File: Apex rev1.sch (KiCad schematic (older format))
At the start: 23 parts, among them J1 OLED, SW1 SW_PUSH, SW2 Rotary_Encoder_Switch, U1 AT90USB1286-MU, Y1 8MHz

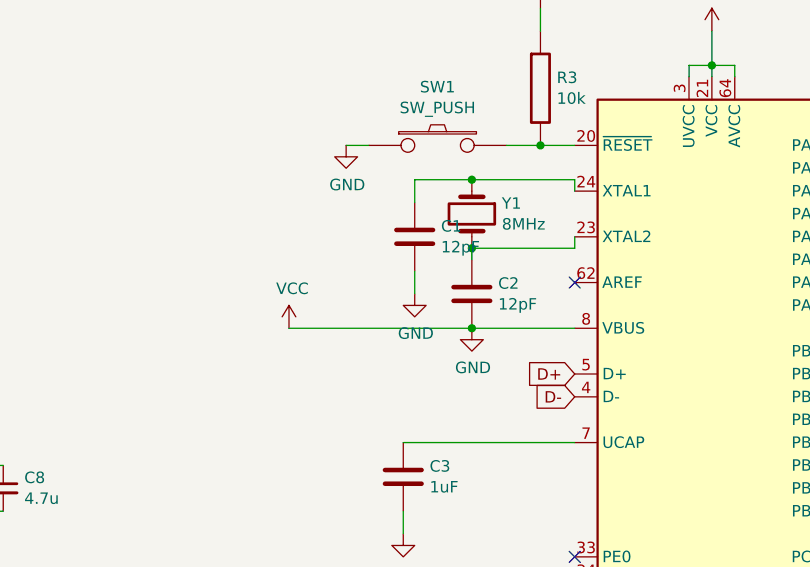
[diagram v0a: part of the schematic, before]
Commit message: Fixed symbols
Re-wired MCU XTAL and corrected footprints
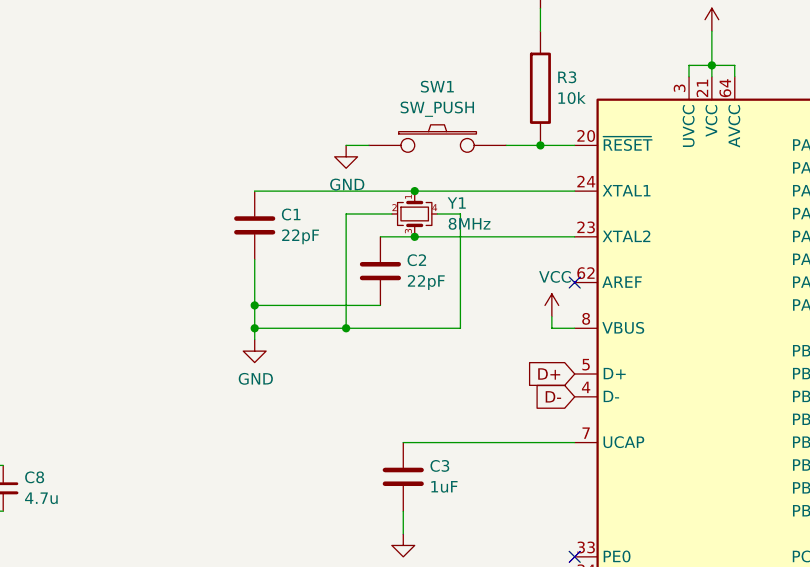
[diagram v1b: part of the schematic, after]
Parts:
- removed Y1: 8MHz, Crystal:Crystal_SMD_0603-2Pin_6.0x3.5mm, symbol Device:Crystal
- added Y1: 8MHz, Crystal:Crystal_SMD_3225-4Pin_3.2x2.5mm, symbol Device:Crystal_GND24_Small
- C1, C2: value 12pF -> 22pF
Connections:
- net GND: now also Y1.2, Y1.4; no longer C4.1, C5.1, C6.1, C7.1, C8.1, R1.1, R2.1, R26.1, R27.1, R3.1, U1.21 (VCC), U1.3 (UVCC), U1.52 (VCC), U1.64 (AVCC), U1.8 (VBUS)
- net at C2.1, U1.23 (XTAL2): now also Y1.3
- net at C1.1, U1.24 (XTAL1): now also Y1.1
- new net VCC: C4.1, C5.1, C6.1, C7.1, C8.1, R1.1, R2.1, R26.1, R27.1, R3.1, U1.21 (VCC), U1.3 (UVCC), U1.52 (VCC), U1.64 (AVCC), U1.8 (VBUS)
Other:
- moved on the sheet: C1, C2
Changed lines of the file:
@@
 	7400 1750 7500 1750
-$Comp
-L Device:Crystal Y1
-U 1 1 5F03BFD9
-P 7950 2050
-F 0 "Y1" V 7904 2181 50  0000 L CNN
-F 1 "8MHz" V 7995 2181 50  0000 L CNN
-F 2 "Crystal:Crystal_SMD_0603-2Pin_6.0x3.5mm" H 7950 2050 50  0001 C CNN
-F 3 "~" H 7950 2050 50  0001 C CNN
-	1    7950 2050
-	0    1    1    0
-$EndComp
-Wire Wire Line
-	8400 1950 8400 1900
-Wire Wire Line
-	8400 1900 7950 1900
-Wire Wire Line
-	7700 1900 7700 2000
-Connection ~ 7950 1900
-Wire Wire Line
-	7950 1900 7700 1900
-Wire Wire Line
-	8400 2150 8400 2200
-Wire Wire Line
-	8400 2200 7950 2200
-Wire Wire Line
-	7950 2200 7950 2250
-Connection ~ 7950 2200
 $Comp
 L Device:C C1
 U 1 1 5F03FC8D
-P 7700 2150
-F 0 "C1" H 7815 2196 50  0000 L CNN
-F 1 "12pF" H 7815 2105 50  0000 L CNN
-F 2 "Capacitor_SMD:C_0805_2012Metric" H 7738 2000 50  0001 C CNN
-F 3 "~" H 7700 2150 50  0001 C CNN
-	1    7700 2150
-	1    0    0    -1
-$EndComp
-Wire Wire Line
-	7700 2300 7700 2400
+P 7000 2100
+F 0 "C1" H 7115 2146 50  0000 L CNN
+F 1 "22pF" H 7115 2055 50  0000 L CNN
+F 2 "Capacitor_SMD:C_0805_2012Metric" H 7038 1950 50  0001 C CNN
+F 3 "~" H 7000 2100 50  0001 C CNN
+	1    7000 2100
+	1    0    0    -1
+$EndComp
 $Comp
 L Device:C C2
 U 1 1 5F0408BF
-P 7950 2400
-F 0 "C2" H 8065 2446 50  0000 L CNN
-F 1 "12pF" H 8065 2355 50  0000 L CNN
-F 2 "Capacitor_SMD:C_0805_2012Metric" H 7988 2250 50  0001 C CNN
-F 3 "~" H 7950 2400 50  0001 C CNN
-	1    7950 2400
-	1    0    0    -1
-$EndComp
-$Comp
-L power:GND #PWR0104
-U 1 1 5F0414EA
-P 7700 2400
-F 0 "#PWR0104" H 7700 2150 50  0001 C CNN
-F 1 "GND" H 7705 2227 50  0000 C CNN
-F 2 "" H 7700 2400 50  0001 C CNN
-F 3 "" H 7700 2400 50  0001 C CNN
-	1    7700 2400
+P 7550 2300
+F 0 "C2" H 7665 2346 50  0000 L CNN
+F 1 "22pF" H 7665 2255 50  0000 L CNN
+F 2 "Capacitor_SMD:C_0805_2012Metric" H 7588 2150 50  0001 C CNN
+F 3 "~" H 7550 2300 50  0001 C CNN
+	1    7550 2300
 	1    0    0    -1
 $EndComp
@@
 L power:GND #PWR0105
 U 1 1 5F041BDD
-P 7950 2550
-F 0 "#PWR0105" H 7950 2300 50  0001 C CNN
-F 1 "GND" H 7955 2377 50  0000 C CNN
-F 2 "" H 7950 2550 50  0001 C CNN
-F 3 "" H 7950 2550 50  0001 C CNN
-	1    7950 2550
+P 7000 2600
+F 0 "#PWR0105" H 7000 2350 50  0001 C CNN
+F 1 "GND" H 7005 2427 50  0000 C CNN
+F 2 "" H 7000 2600 50  0001 C CNN
+F 3 "" H 7000 2600 50  0001 C CNN
+	1    7000 2600
 	1    0    0    -1
 $EndComp
@@
 	1    0    0    -1
 $EndComp
-Wire Wire Line
-	8400 2550 7950 2550
-Connection ~ 7950 2550
-Wire Wire Line
-	7950 2550 7150 2550
 $Comp
 L power:VCC #PWR0112
 U 1 1 5F073B72
-P 7150 2550
-F 0 "#PWR0112" H 7150 2400 50  0001 C CNN
-F 1 "VCC" H 7165 2723 50  0000 C CNN
-F 2 "" H 7150 2550 50  0001 C CNN
-F 3 "" H 7150 2550 50  0001 C CNN
-	1    7150 2550
+P 8300 2500
+F 0 "#PWR0112" H 8300 2350 50  0001 C CNN
+F 1 "VCC" H 8315 2673 50  0000 C CNN
+F 2 "" H 8300 2500 50  0001 C CNN
+F 3 "" H 8300 2500 50  0001 C CNN
+	1    8300 2500
 	1    0    0    -1
 $EndComp
@@
 NoConn ~ 9600 2250
 NoConn ~ 9600 2350
+Wire Wire Line
+	8400 2550 8300 2550
+Wire Wire Line
+	8300 2550 8300 2500
+Wire Wire Line
+	8400 1950 7700 1950
+Wire Wire Line
+	8400 2150 7700 2150
+$Comp
+L Device:Crystal_GND24_Small Y1
+U 1 1 5F0E2CAB
+P 7700 2050
+F 0 "Y1" V 7654 2194 50  0000 L CNN
+F 1 "8MHz" V 7745 2194 50  0000 L CNN
+F 2 "Crystal:Crystal_SMD_3225-4Pin_3.2x2.5mm" H 7700 2050 50  0001 C CNN
+F 3 "~" H 7700 2050 50  0001 C CNN
+	1    7700 2050
+	0    1    1    0
+$EndComp
+Connection ~ 7700 1950
+Wire Wire Line
+	7700 1950 7000 1950
+Wire Wire Line
+	7700 2150 7550 2150
+Connection ~ 7700 2150
+Wire Wire Line
+	7000 2250 7000 2450
+Wire Wire Line
+	7550 2450 7000 2450
+Wire Wire Line
+	7000 2450 7000 2550
+Connection ~ 7000 2450
+Wire Wire Line
+	7600 2050 7400 2050
+Wire Wire Line
+	7400 2050 7400 2550
+Wire Wire Line
+	7400 2550 7900 2550
+Wire Wire Line
+	7900 2550 7900 2050
+Wire Wire Line
+	7900 2050 7800 2050
+Wire Wire Line
+	7400 2550 7000 2550
+Connection ~ 7400 2550
+Connection ~ 7000 2550
+Wire Wire Line
+	7000 2550 7000 2600
 $EndSCHEMATC

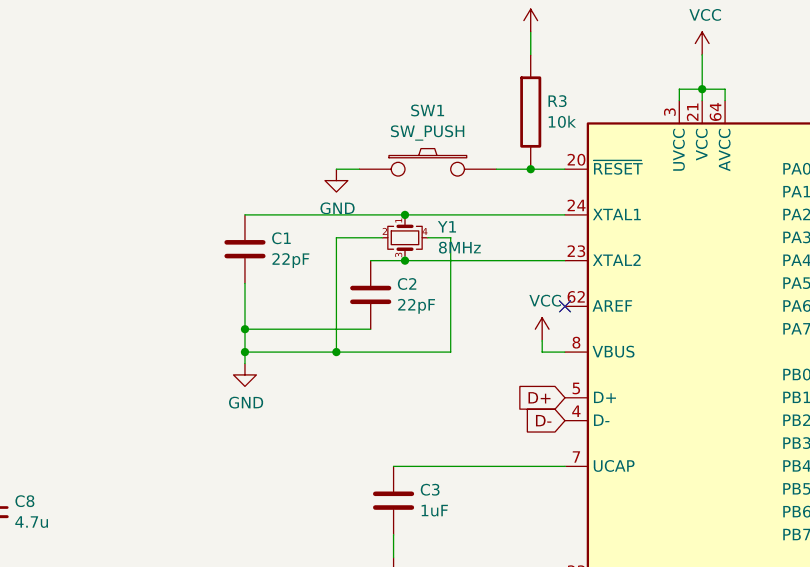
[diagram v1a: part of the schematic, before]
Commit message: reworked crystal
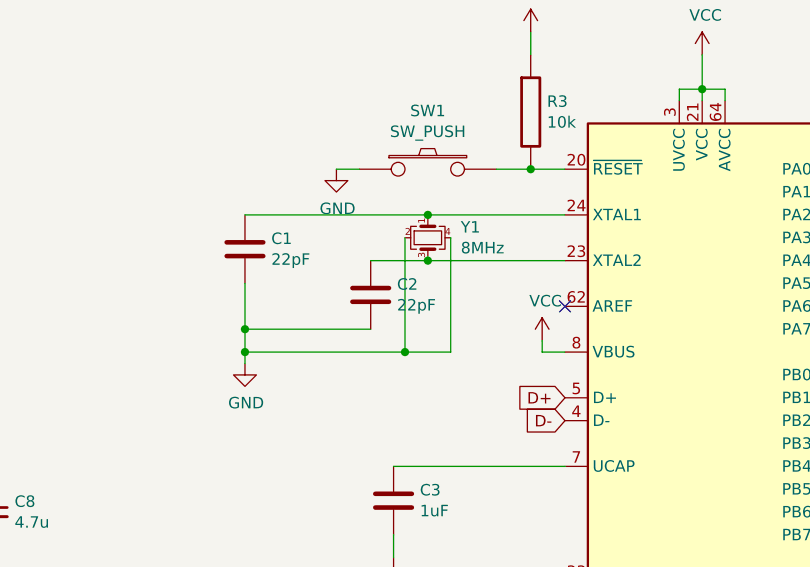
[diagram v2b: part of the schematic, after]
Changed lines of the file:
@@
 	8300 2550 8300 2500
-Wire Wire Line
-	8400 1950 7700 1950
-Wire Wire Line
-	8400 2150 7700 2150
-$Comp
-L Device:Crystal_GND24_Small Y1
-U 1 1 5F0E2CAB
-P 7700 2050
-F 0 "Y1" V 7654 2194 50  0000 L CNN
-F 1 "8MHz" V 7745 2194 50  0000 L CNN
-F 2 "Crystal:Crystal_SMD_3225-4Pin_3.2x2.5mm" H 7700 2050 50  0001 C CNN
-F 3 "~" H 7700 2050 50  0001 C CNN
-	1    7700 2050
-	0    1    1    0
-$EndComp
-Connection ~ 7700 1950
-Wire Wire Line
-	7700 1950 7000 1950
-Wire Wire Line
-	7700 2150 7550 2150
-Connection ~ 7700 2150
 Wire Wire Line
 	7000 2250 7000 2450
 Wire Wire Line
 	7550 2450 7000 2450
+Connection ~ 7000 2450
 Wire Wire Line
 	7000 2450 7000 2550
-Connection ~ 7000 2450
 Wire Wire Line
-	7600 2050 7400 2050
+	7000 1950 7800 1950
 Wire Wire Line
-	7400 2050 7400 2550
+	7550 2150 7800 2150
+$Comp
+L Device:Crystal_GND24_Small Y1
+U 1 1 5F1F04E2
+P 7800 2050
+F 0 "Y1" V 7754 2194 50  0000 L CNN
+F 1 "8MHz" V 7845 2194 50  0000 L CNN
+F 2 "Crystal:Crystal_SMD_3225-4Pin_3.2x2.5mm" H 7800 2050 50  0001 C CNN
+F 3 "~" H 7800 2050 50  0001 C CNN
+	1    7800 2050
+	0    1    1    0
+$EndComp
+Connection ~ 7800 2150
 Wire Wire Line
-	7400 2550 7900 2550
+	7800 2150 8400 2150
+Connection ~ 7800 1950
 Wire Wire Line
-	7900 2550 7900 2050
+	7800 1950 8400 1950
 Wire Wire Line
-	7900 2050 7800 2050
+	7900 2050 7900 2550
 Wire Wire Line
-	7400 2550 7000 2550
-Connection ~ 7400 2550
+	7900 2550 7700 2550
+Wire Wire Line
+	7700 2550 7700 2050
+Wire Wire Line
+	7700 2550 7000 2550
+Connection ~ 7700 2550
 Connection ~ 7000 2550
 Wire Wire Line

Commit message: routed crystal area and decoupling caps
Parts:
- removed C7: .1u, Capacitor_SMD:C_0805_2012Metric, symbol Device:C_Small
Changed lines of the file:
@@
-$EndComp
-$Comp
-L Device:C_Small C7
-U 1 1 5F0A2EEA
-P 5450 3250
-F 0 "C7" H 5542 3296 50  0000 L CNN
-F 1 ".1u" H 5542 3205 50  0000 L CNN
-F 2 "Capacitor_SMD:C_0805_2012Metric" H 5450 3250 50  0001 C CNN
-F 3 "~" H 5450 3250 50  0001 C CNN
-	1    5450 3250
-	1    0    0    -1
 $EndComp
 $Comp
@@
 	4550 3150 5000 3150
 Connection ~ 5000 3150
-Wire Wire Line
-	5000 3150 5450 3150
-Connection ~ 5450 3150
-Wire Wire Line
-	5450 3150 5900 3150
-Wire Wire Line
-	5900 3350 5450 3350
 Connection ~ 4550 3350
 Wire Wire Line
@@
 Wire Wire Line
 	5000 3350 4550 3350
-Connection ~ 5450 3350
-Wire Wire Line
-	5450 3350 5000 3350
 Wire Wire Line
 	4200 3350 4200 3450
@@
 Wire Wire Line
 	7000 2550 7000 2600
+Wire Wire Line
+	5000 3150 5900 3150
+Wire Wire Line
+	5000 3350 5900 3350
 $EndSCHEMATC

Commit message: assigned some pins
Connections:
- net ROT1: now also U1.19 (PE5)
- net ROT2: now also U1.18 (PE4)
- net COL16: now reaches U1.27 (PD2)
- net ROW5: now reaches U1.28 (PD3)
- net COL15: now reaches U1.30 (PD5)
- net ROW4: now reaches U1.32 (PD7)
- net COL14: now reaches U1.58 (PF3)
- net ROW2: now reaches U1.60 (PF1)
- net ROW1: now reaches U1.61 (PF0)
- net ENC1: no longer names the net of C25.1, R28.2
- net ENC2: no longer names the net of C26.1, R29.2
- no-connect marks 43 -> 34
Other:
- moved on the sheet: R4
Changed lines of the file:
@@
 $EndComp
 Wire Wire Line
-	8400 3750 8150 3750
-Wire Wire Line
-	8150 3750 8150 3900
+	7750 3750 7750 3900
 $Comp
 L Device:R R4
 U 1 1 5F0438EB
-P 8150 4050
-F 0 "R4" H 8220 4096 50  0000 L CNN
-F 1 "1k" H 8220 4005 50  0000 L CNN
-F 2 "1_Keyboard Footprints:R_0603" V 8080 4050 50  0001 C CNN
-F 3 "~" H 8150 4050 50  0001 C CNN
-	1    8150 4050
+P 7750 4050
+F 0 "R4" H 7820 4096 50  0000 L CNN
+F 1 "1k" H 7820 4005 50  0000 L CNN
+F 2 "1_Keyboard Footprints:R_0603" V 7680 4050 50  0001 C CNN
+F 3 "~" H 7750 4050 50  0001 C CNN
+	1    7750 4050
 	1    0    0    -1
 $EndComp
@@
 L power:GND #PWR0107
 U 1 1 5F0441E1
-P 8150 4200
-F 0 "#PWR0107" H 8150 3950 50  0001 C CNN
-F 1 "GND" H 8155 4027 50  0000 C CNN
-F 2 "" H 8150 4200 50  0001 C CNN
-F 3 "" H 8150 4200 50  0001 C CNN
-	1    8150 4200
+P 7750 4200
+F 0 "#PWR0107" H 7750 3950 50  0001 C CNN
+F 1 "GND" H 7755 4027 50  0000 C CNN
+F 2 "" H 7750 4200 50  0001 C CNN
+F 3 "" H 7750 4200 50  0001 C CNN
+	1    7750 4200
 	1    0    0    -1
 $EndComp
@@
 Wire Wire Line
 	12950 3250 12950 3400
-Wire Wire Line
-	12950 3750 12950 3900
-Wire Wire Line
-	12450 3750 12450 3900
 $Comp
 L Device:C_Small C25
@@
 Wire Wire Line
 	12950 3400 12950 3550
-Wire Wire Line
-	12450 3900 12300 3900
-Connection ~ 12450 3900
-Wire Wire Line
-	12450 3900 12450 3950
-Wire Wire Line
-	12950 3900 13100 3900
-Connection ~ 12950 3900
-Wire Wire Line
-	12950 3900 12950 3950
-Text GLabel 12300 3900 0    50   Input ~ 0
-ENC1
-Text GLabel 13100 3900 2    50   Input ~ 0
-ENC2
 $Comp
 L power:GND #PWR0148
@@
 NoConn ~ 8400 3650
 NoConn ~ 8400 3850
-NoConn ~ 8400 3950
-NoConn ~ 8400 4050
+NoConn ~ 9600 3150
 NoConn ~ 8400 4150
 NoConn ~ 8400 4250
-NoConn ~ 8400 4450
-NoConn ~ 8400 4550
 NoConn ~ 8400 4650
-NoConn ~ 8400 4750
 NoConn ~ 8400 4850
 NoConn ~ 8400 4950
 NoConn ~ 8400 5050
 NoConn ~ 8400 5150
-NoConn ~ 9600 5150
 NoConn ~ 9600 5050
-NoConn ~ 9600 4950
 NoConn ~ 9600 4850
-NoConn ~ 9600 4750
-NoConn ~ 9600 4650
 NoConn ~ 9600 4250
 NoConn ~ 9600 4150
@@
 NoConn ~ 9600 3550
 NoConn ~ 9600 3350
-NoConn ~ 9600 3250
-NoConn ~ 9600 3150
 NoConn ~ 9600 3050
 NoConn ~ 9600 2650
@@
 Wire Wire Line
 	5000 3350 5900 3350
+Text GLabel 8400 4050 0    50   Input ~ 0
+ROT1
+Text GLabel 8400 3950 0    50   Input ~ 0
+ROT2
+Wire Wire Line
+	12450 3750 12450 3950
+Wire Wire Line
+	12950 3750 12950 3950
+Wire Wire Line
+	7750 3750 8400 3750
+NoConn ~ 9600 3250
+Text GLabel 9600 4650 2    50   Input ~ 0
+COL16
+Text GLabel 9600 4750 2    50   Input ~ 0
+ROW5
+Text GLabel 9600 4950 2    50   Input ~ 0
+COL15
+Text GLabel 9600 5150 2    50   Input ~ 0
+ROW4
+Text GLabel 8400 4750 0    50   Input ~ 0
+COL14
+Text GLabel 8400 4450 0    50   Input ~ 0
+ROW1
+Text GLabel 8400 4550 0    50   Input ~ 0
+ROW2
 $EndSCHEMATC

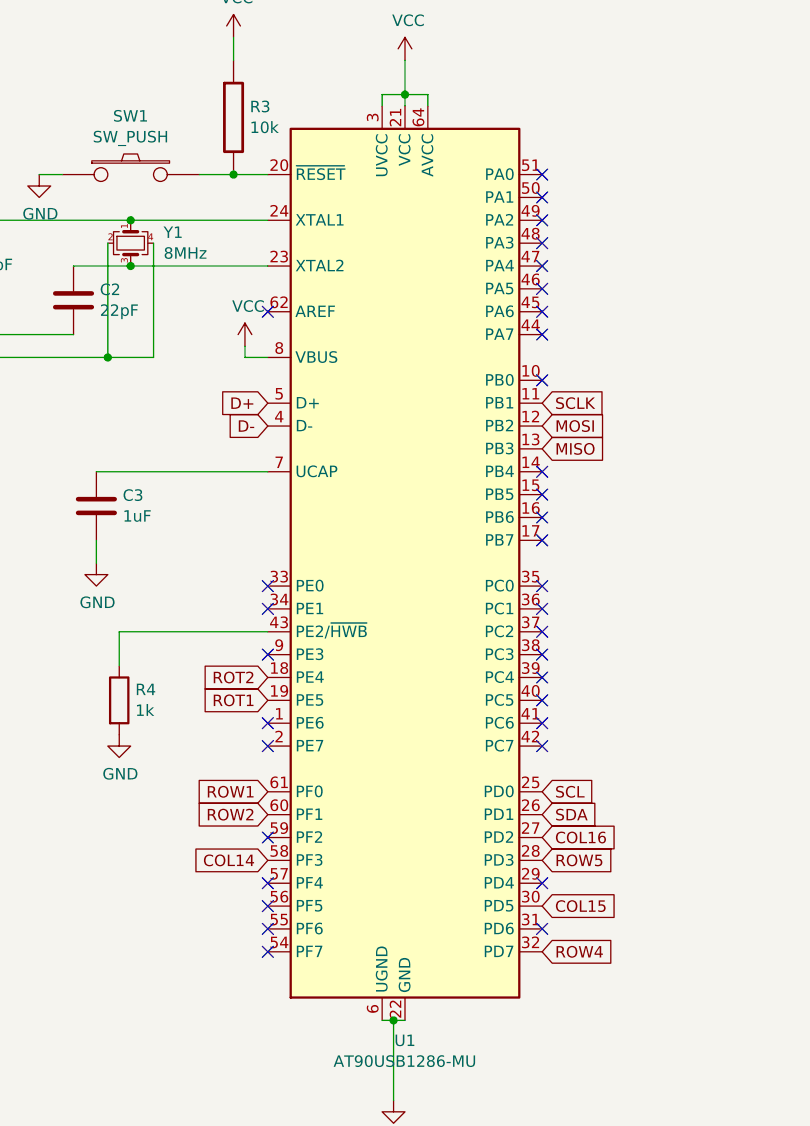
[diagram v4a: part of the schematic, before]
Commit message: completed routing matrix
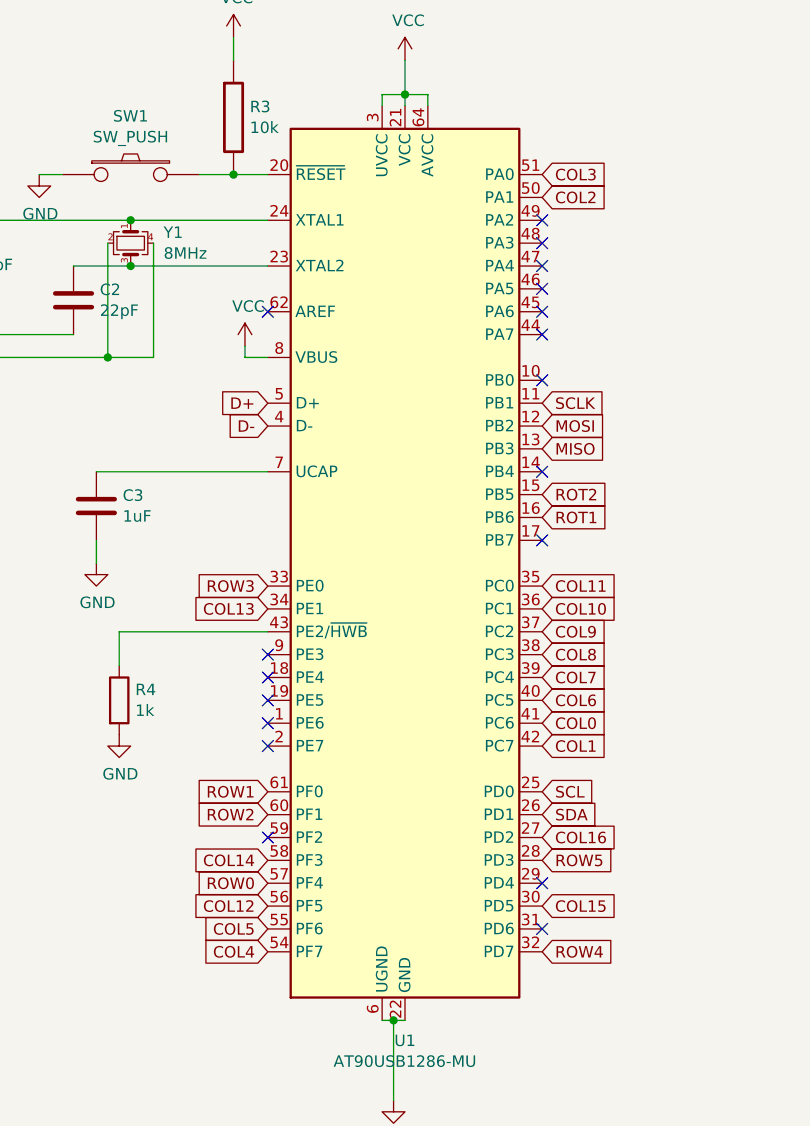
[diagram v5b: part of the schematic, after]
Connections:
- net ROT1: now also U1.16 (PB6); no longer U1.19 (PE5)
- net ROT2: now also U1.15 (PB5); no longer U1.18 (PE4)
- net ROW3: now reaches U1.33 (PE0)
- net COL13: now reaches U1.34 (PE1)
- net COL11: now reaches U1.35 (PC0)
- net COL10: now reaches U1.36 (PC1)
- net COL9: now reaches U1.37 (PC2)
- net COL8: now reaches U1.38 (PC3)
- net COL7: now reaches U1.39 (PC4)
- net COL6: now reaches U1.40 (PC5)
- net COL0: now reaches U1.41 (PC6)
- net COL1: now reaches U1.42 (PC7)
- net COL2: now reaches U1.50 (PA1)
- net COL3: now reaches U1.51 (PA0)
- net COL4: now reaches U1.54 (PF7)
- net COL5: now reaches U1.55 (PF6)
- net COL12: now reaches U1.56 (PF5)
- net ROW0: now reaches U1.57 (PF4)
- no-connect marks 34 -> 18
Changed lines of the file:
@@
 $EndComp
 NoConn ~ 8400 2350
-NoConn ~ 8400 3550
-NoConn ~ 8400 3650
 NoConn ~ 8400 3850
-NoConn ~ 9600 3150
+NoConn ~ 8400 4050
 NoConn ~ 8400 4150
 NoConn ~ 8400 4250
 NoConn ~ 8400 4650
-NoConn ~ 8400 4850
-NoConn ~ 8400 4950
-NoConn ~ 8400 5050
-NoConn ~ 8400 5150
 NoConn ~ 9600 5050
 NoConn ~ 9600 4850
-NoConn ~ 9600 4250
-NoConn ~ 9600 4150
-NoConn ~ 9600 4050
-NoConn ~ 9600 3950
-NoConn ~ 9600 3850
-NoConn ~ 9600 3750
-NoConn ~ 9600 3650
-NoConn ~ 9600 3550
 NoConn ~ 9600 3350
-NoConn ~ 9600 3050
+NoConn ~ 8400 3950
 NoConn ~ 9600 2650
 NoConn ~ 9600 2450
-NoConn ~ 9600 1750
-NoConn ~ 9600 1850
 NoConn ~ 9600 1950
 NoConn ~ 9600 2050
@@
 Wire Wire Line
 	5000 3350 5900 3350
-Text GLabel 8400 4050 0    50   Input ~ 0
+Text GLabel 9600 3250 2    50   Input ~ 0
 ROT1
-Text GLabel 8400 3950 0    50   Input ~ 0
+Text GLabel 9600 3150 2    50   Input ~ 0
 ROT2
 Wire Wire Line
@@
 Wire Wire Line
 	7750 3750 8400 3750
-NoConn ~ 9600 3250
+NoConn ~ 9600 3050
 Text GLabel 9600 4650 2    50   Input ~ 0
 COL16
@@
 Text GLabel 8400 4550 0    50   Input ~ 0
 ROW2
+Text GLabel 8400 4850 0    50   Input ~ 0
+ROW0
+Text GLabel 8400 3550 0    50   Input ~ 0
+ROW3
+Text GLabel 8400 3650 0    50   Input ~ 0
+COL13
+Text GLabel 8400 4950 0    50   Input ~ 0
+COL12
+Text GLabel 9600 3650 2    50   Input ~ 0
+COL10
+Text GLabel 9600 3750 2    50   Input ~ 0
+COL9
+Text GLabel 9600 3850 2    50   Input ~ 0
+COL8
+Text GLabel 9600 3550 2    50   Input ~ 0
+COL11
+Text GLabel 9600 3950 2    50   Input ~ 0
+COL7
+Text GLabel 9600 4050 2    50   Input ~ 0
+COL6
+Text GLabel 9600 4150 2    50   Input ~ 0
+COL0
+Text GLabel 9600 4250 2    50   Input ~ 0
+COL1
+Text GLabel 8400 5050 0    50   Input ~ 0
+COL5
+Text GLabel 8400 5150 0    50   Input ~ 0
+COL4
+Text GLabel 9600 1750 2    50   Input ~ 0
+COL3
+Text GLabel 9600 1850 2    50   Input ~ 0
+COL2
 $EndSCHEMATC
